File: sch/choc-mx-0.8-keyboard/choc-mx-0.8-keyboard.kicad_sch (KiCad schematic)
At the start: 1 part, among them U1 Pico

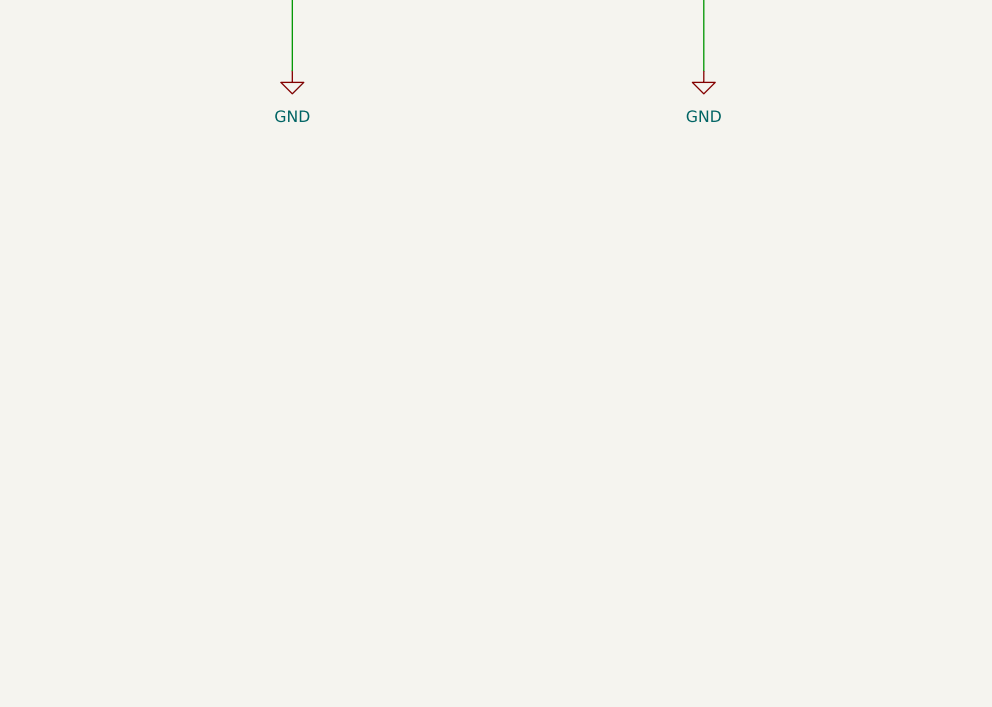
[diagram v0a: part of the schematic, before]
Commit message: AE-RP2040も使えるようにしました。
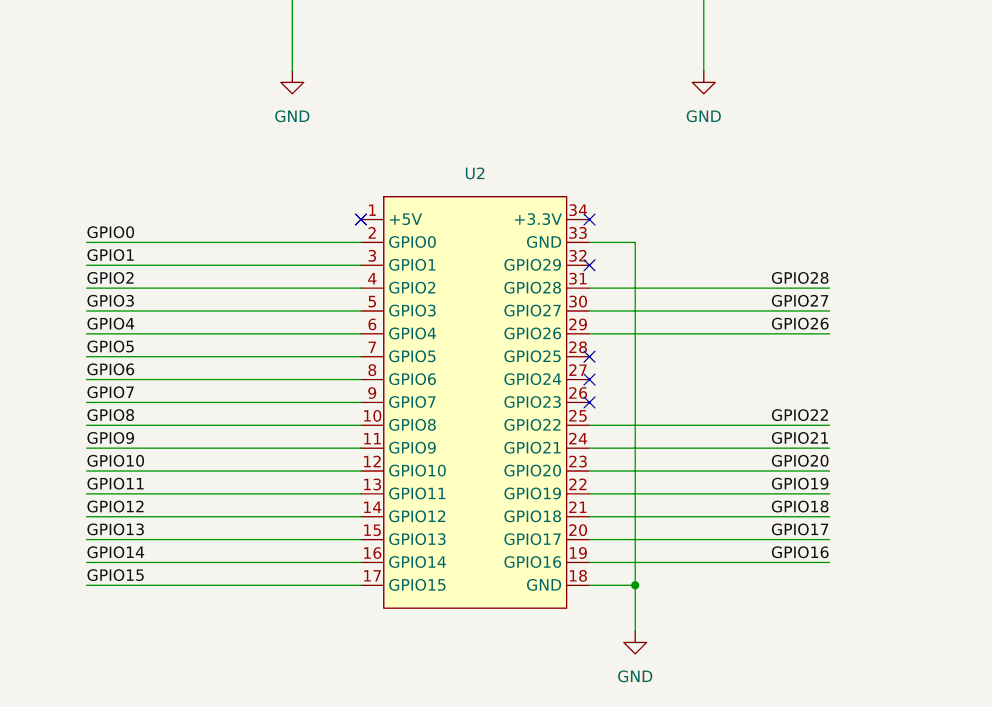
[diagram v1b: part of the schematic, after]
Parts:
- added U2: ~, ae-rp2040:AE-RP2040, symbol ae-rp2040:AE-RP2040
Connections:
- net GND: now also U2.18 (GND), U2.33 (GND)
- net GPIO0: now also U2.2 (GPIO0)
- net GPIO1: now also U2.3 (GPIO1)
- net GPIO10: now also U2.12 (GPIO10)
- net GPIO11: now also U2.13 (GPIO11)
- net GPIO12: now also U2.14 (GPIO12)
- net GPIO13: now also U2.15 (GPIO13)
- net GPIO14: now also U2.16 (GPIO14)
- net GPIO15: now also U2.17 (GPIO15)
- net GPIO16: now also U2.19 (GPIO16)
- net GPIO17: now also U2.20 (GPIO17)
- net GPIO18: now also U2.21 (GPIO18)
- net GPIO19: now also U2.22 (GPIO19)
- net GPIO2: now also U2.4 (GPIO2)
- net GPIO20: now also U2.23 (GPIO20)
- net GPIO21: now also U2.24 (GPIO21)
- net GPIO22: now also U2.25 (GPIO22)
- net GPIO26: now also U2.29 (GPIO26)
- net GPIO27: now also U2.30 (GPIO27)
- net GPIO28: now also U2.31 (GPIO28)
- net GPIO3: now also U2.5 (GPIO3)
- net GPIO4: now also U2.6 (GPIO4)
- net GPIO5: now also U2.7 (GPIO5)
- net GPIO6: now also U2.8 (GPIO6)
- net GPIO7: now also U2.9 (GPIO7)
- net GPIO8: now also U2.10 (GPIO8)
- net GPIO9: now also U2.11 (GPIO9)
- no-connect marks 6 -> 12
